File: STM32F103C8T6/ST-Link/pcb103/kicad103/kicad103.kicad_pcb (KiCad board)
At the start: 4 copper layers, 82 x 52 mm, 32 parts, among them IC1 LD1117DT33TR, J1 0480372200, J2 Conn_01x02_Socket, J3 Conn_02x05_Odd_Even, J5 Conn_01x16_Pin, J7 Conn_01x04_Pin, J8 Conn_01x05_Socket, J9 Conn_01x17_Pin, U1 STM32F103C8T6, Y1 8MHz 20pF

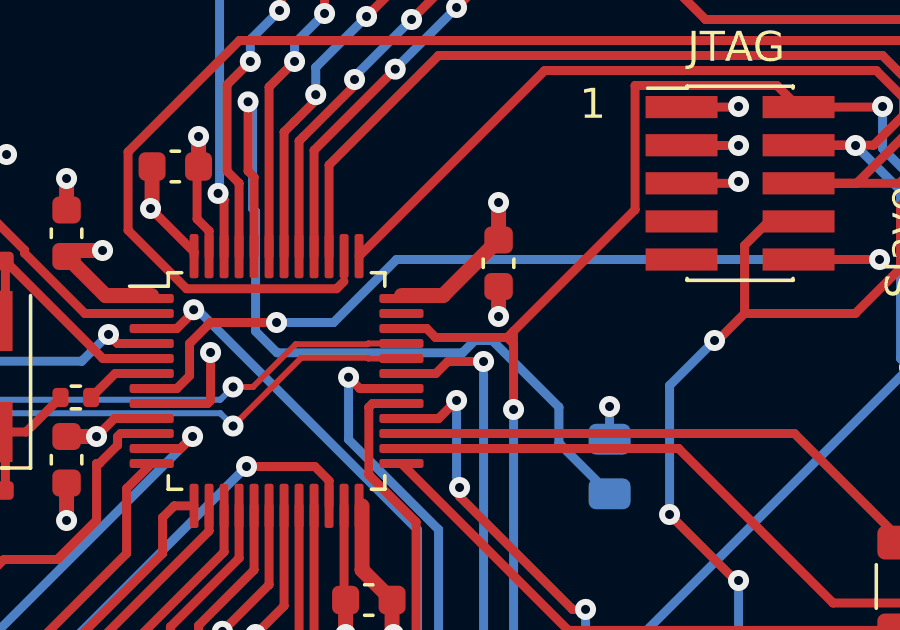
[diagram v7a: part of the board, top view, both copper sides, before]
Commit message: Connect missing GND
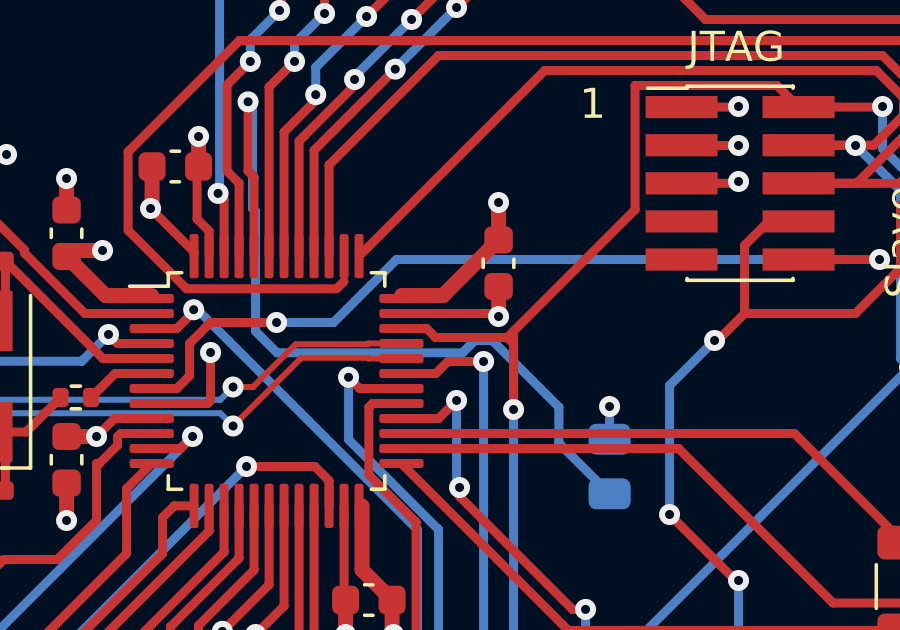
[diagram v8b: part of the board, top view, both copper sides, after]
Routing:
- net GND: track 40.6 -> 43.9 mm
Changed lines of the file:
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@@
   (segment (start 100.4 60.3) (end 98.51 60.3) (width 0.3) (layer "F.Cu") (net 4))
   (segment (start 100.34 61.56) (end 100.4 61.5) (width 0.3) (layer "F.Cu") (net 4))
+  (segment (start 92.3 65.9) (end 92.4 66) (width 0.3) (layer "F.Cu") (net 4))
   (segment (start 92.4 65) (end 92.4 66) (width 0.5) (layer "F.Cu") (net 4))
   (segment (start 100.3 60.29) (end 100.29 60.29) (width 0.3) (layer "F.Cu") (net 4))
@@
   (segment (start 78 71.55) (end 78 72.8) (width 0.5) (layer "F.Cu") (net 4))
   (segment (start 75 64.15) (end 74.25 64.15) (width 0.5) (layer "F.Cu") (net 4))
+  (segment (start 89.1625 65.9) (end 92.3 65.9) (width 0.3) (layer "F.Cu") (net 4))
   (segment (start 100.4 60.3) (end 100.3 60.29) (width 0.3) (layer "F.Cu") (net 4))
   (segment (start 82.4 61) (end 82.4 60) (width 0.5) (layer "F.Cu") (net 4))
